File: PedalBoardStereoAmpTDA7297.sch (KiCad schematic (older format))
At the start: 17 parts, among them J1 OUT-L, J2 IN-L, J3 OUT-R, J4 IN-R, J5 PWR, U1 TDA7297

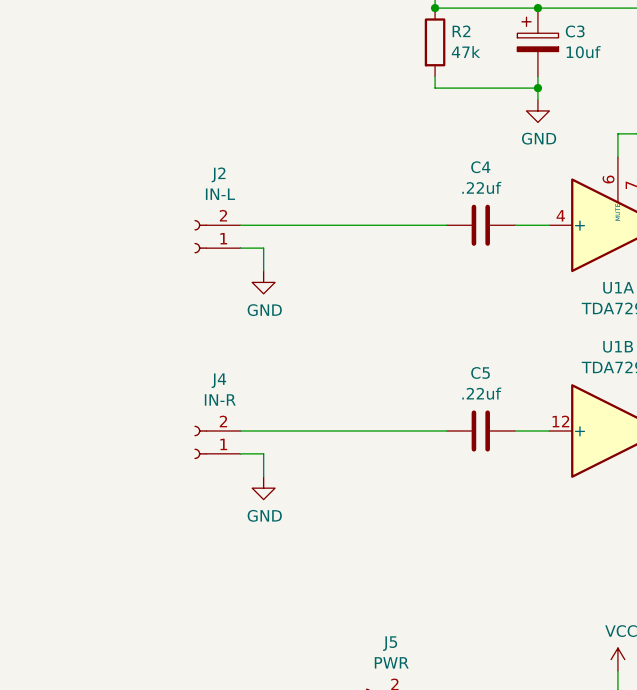
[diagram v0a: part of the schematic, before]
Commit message: update with pots connector
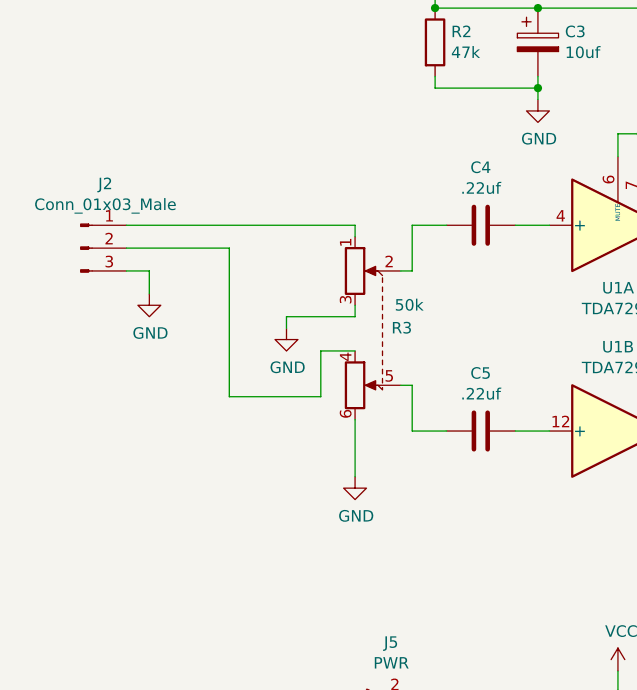
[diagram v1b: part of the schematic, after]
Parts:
- removed J2: IN-L, Connector_PinHeader_2.54mm:PinHeader_1x02_P2.54mm_Vertical, symbol Connector:Conn_01x02_Female
- removed J4: IN-R, Connector_PinHeader_2.54mm:PinHeader_1x02_P2.54mm_Vertical, symbol Connector:Conn_01x02_Female
- added J2: Conn_01x03_Male, Connector_PinHeader_2.54mm:PinHeader_1x03_P2.54mm_Vertical, symbol Connector:Conn_01x03_Male
- added R3: 50k, Connector_PinHeader_2.54mm:PinHeader_1x06_P2.54mm_Vertical, symbol Device:R_POT_Dual
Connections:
- net GND: now also J2.3 (Pin_3), R3.3, R3.6
- net at C4.2: now also R3.2
- net at C5.2: now also R3.5
- new net: J2.1 (Pin_1), R3.1
- new net: J2.2 (Pin_2), R3.4
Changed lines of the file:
@@
 Wire Wire Line
 	3350 5100 3500 5100
-$Comp
-L Connector:Conn_01x02_Female J2
-U 1 1 5F7EF550
-P 1950 4300
-F 0 "J2" H 1842 3975 50  0000 C CNN
-F 1 "IN-L" H 1842 4066 50  0000 C CNN
-F 2 "Connector_PinHeader_2.54mm:PinHeader_1x02_P2.54mm_Vertical" H 1950 4300 50  0001 C CNN
-F 3 "~" H 1950 4300 50  0001 C CNN
-	1    1950 4300
-	-1   0    0    1
-$EndComp
-Wire Wire Line
-	2150 4200 3050 4200
-Wire Wire Line
-	2150 4300 2250 4300
-Wire Wire Line
-	2250 4300 2250 4400
+Wire Wire Line
+	1650 4400 1750 4400
+Wire Wire Line
+	1750 4400 1750 4500
 $Comp
 L power:GND #PWR07
 U 1 1 5F7F16CE
-P 2250 4400
-F 0 "#PWR07" H 2250 4150 50  0001 C CNN
-F 1 "GND" H 2255 4227 50  0000 C CNN
-F 2 "" H 2250 4400 50  0001 C CNN
-F 3 "" H 2250 4400 50  0001 C CNN
-	1    2250 4400
-	1    0    0    -1
-$EndComp
-$Comp
-L Connector:Conn_01x02_Female J4
-U 1 1 5F7F2F23
-P 1950 5200
-F 0 "J4" H 1842 4875 50  0000 C CNN
-F 1 "IN-R" H 1842 4966 50  0000 C CNN
-F 2 "Connector_PinHeader_2.54mm:PinHeader_1x02_P2.54mm_Vertical" H 1950 5200 50  0001 C CNN
-F 3 "~" H 1950 5200 50  0001 C CNN
-	1    1950 5200
-	-1   0    0    1
-$EndComp
-Wire Wire Line
-	2150 5100 3050 5100
-Wire Wire Line
-	2150 5200 2250 5200
-Wire Wire Line
-	2250 5200 2250 5300
-$Comp
-L power:GND #PWR08
-U 1 1 5F7F2F42
-P 2250 5300
-F 0 "#PWR08" H 2250 5050 50  0001 C CNN
-F 1 "GND" H 2255 5127 50  0000 C CNN
-F 2 "" H 2250 5300 50  0001 C CNN
-F 3 "" H 2250 5300 50  0001 C CNN
-	1    2250 5300
+P 1750 4500
+F 0 "#PWR07" H 1750 4250 50  0001 C CNN
+F 1 "GND" H 1755 4327 50  0000 C CNN
+F 2 "" H 1750 4500 50  0001 C CNN
+F 3 "" H 1750 4500 50  0001 C CNN
+	1    1750 4500
 	1    0    0    -1
 $EndComp
@@
 	1    0    0    -1
 $EndComp
+$Comp
+L Device:R_POT_Dual R3
+U 1 1 5F8D8A34
+P 2750 4650
+F 0 "R3" V 2750 4800 50  0000 R CNN
+F 1 "50k" V 2650 4850 50  0000 R CNN
+F 2 "Connector_PinHeader_2.54mm:PinHeader_1x06_P2.54mm_Vertical" H 3000 4575 50  0001 C CNN
+F 3 "~" H 3000 4575 50  0001 C CNN
+	1    2750 4650
+	0    1    1    0
+$EndComp
+Wire Wire Line
+	2850 4400 2900 4400
+Wire Wire Line
+	2900 4400 2900 4200
+Wire Wire Line
+	2900 4200 3050 4200
+Wire Wire Line
+	2850 4900 2900 4900
+Wire Wire Line
+	2900 4900 2900 5100
+Wire Wire Line
+	2900 5100 3050 5100
+Wire Wire Line
+	1650 4200 2650 4200
+Wire Wire Line
+	2650 4200 2650 4250
+$Comp
+L power:GND #PWR012
+U 1 1 5F8F5B27
+P 2650 5300
+F 0 "#PWR012" H 2650 5050 50  0001 C CNN
+F 1 "GND" H 2655 5127 50  0000 C CNN
+F 2 "" H 2650 5300 50  0001 C CNN
+F 3 "" H 2650 5300 50  0001 C CNN
+	1    2650 5300
+	1    0    0    -1
+$EndComp
+Wire Wire Line
+	2650 5050 2650 5300
+$Comp
+L power:GND #PWR011
+U 1 1 5F8F79D5
+P 2350 4650
+F 0 "#PWR011" H 2350 4400 50  0001 C CNN
+F 1 "GND" H 2355 4477 50  0000 C CNN
+F 2 "" H 2350 4650 50  0001 C CNN
+F 3 "" H 2350 4650 50  0001 C CNN
+	1    2350 4650
+	1    0    0    -1
+$EndComp
+Wire Wire Line
+	2650 4550 2650 4600
+Wire Wire Line
+	2650 4600 2350 4600
+Wire Wire Line
+	2350 4600 2350 4650
+Wire Wire Line
+	2650 4750 2500 4750
+Wire Wire Line
+	2500 4750 2500 4950
+Wire Wire Line
+	2500 4950 2100 4950
+$Comp
+L Connector:Conn_01x03_Male J2
+U 1 1 5F9626D1
+P 1450 4300
+F 0 "J2" H 1558 4581 50  0000 C CNN
+F 1 "Conn_01x03_Male" H 1558 4490 50  0000 C CNN
+F 2 "Connector_PinHeader_2.54mm:PinHeader_1x03_P2.54mm_Vertical" H 1450 4300 50  0001 C CNN
+F 3 "~" H 1450 4300 50  0001 C CNN
+	1    1450 4300
+	1    0    0    -1
+$EndComp
+Wire Wire Line
+	1650 4300 2100 4300
+Wire Wire Line
+	2100 4300 2100 4950
 $EndSCHEMATC
